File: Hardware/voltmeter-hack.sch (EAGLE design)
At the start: 18 parts, among them IC1 STM32F003F3, IC2 HT7133-1

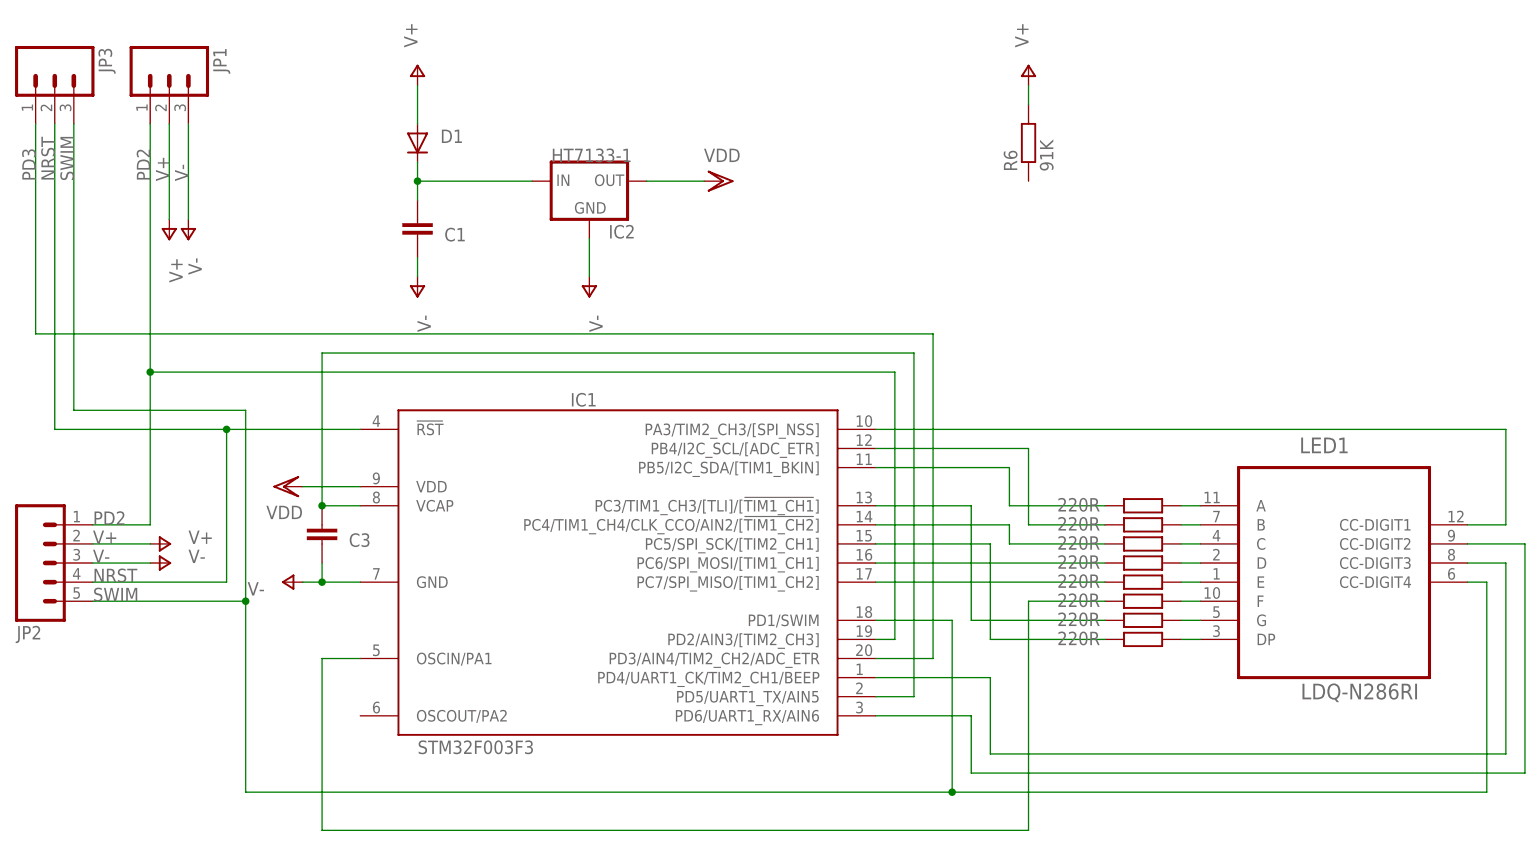
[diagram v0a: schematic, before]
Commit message: hacked voltmeter headers
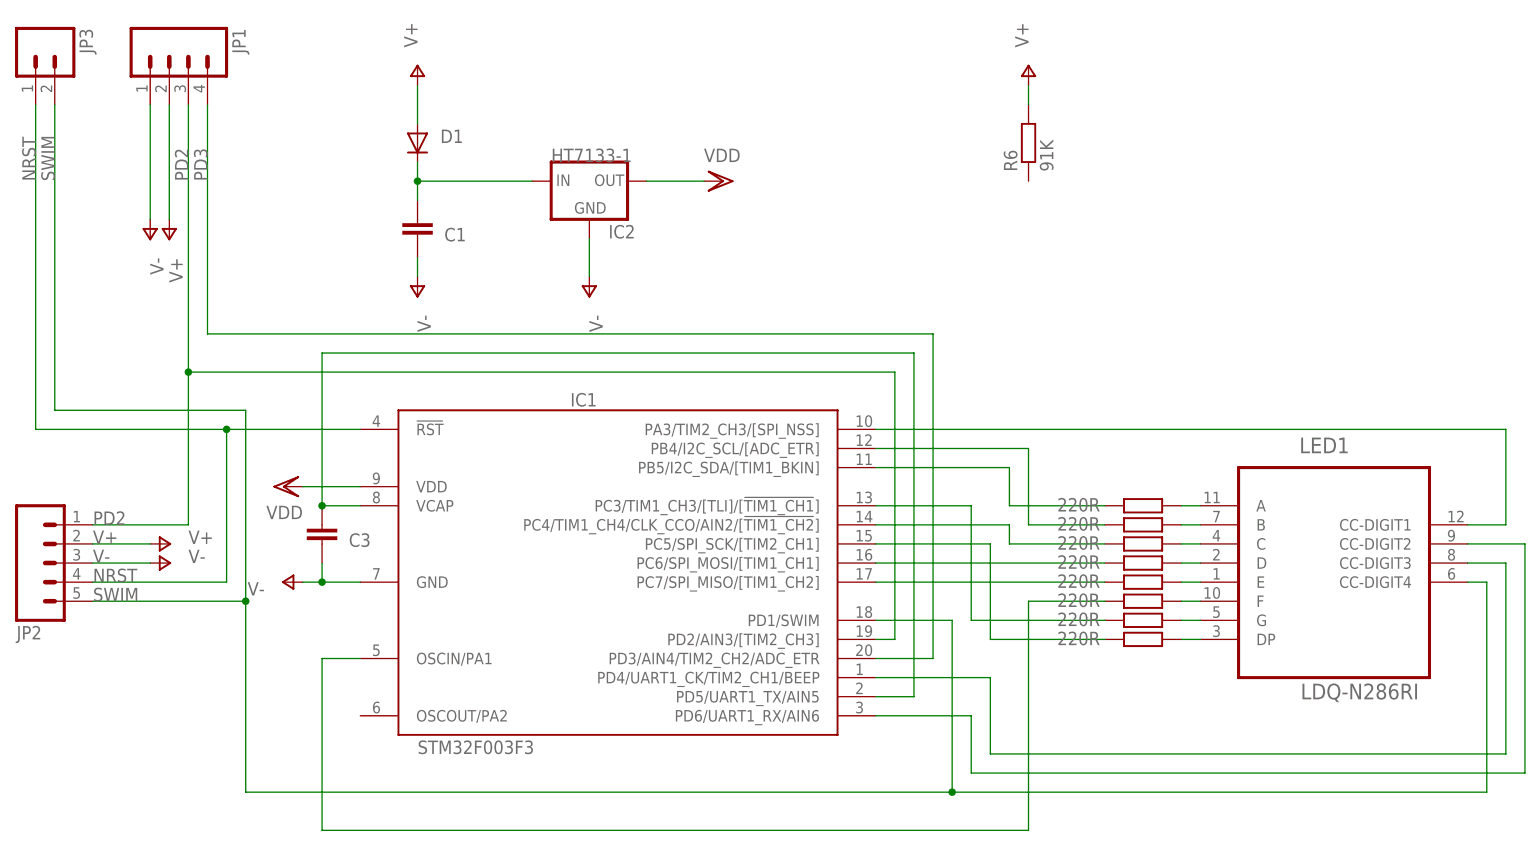
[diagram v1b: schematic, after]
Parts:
- JP1: device SparkFun:M03PTH -> SparkFun:M04PTH
- JP3: device SparkFun:M03PTH -> SparkFun:M02PTH
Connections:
- net NRST: now also JP3.1; no longer JP3.2
- net PD2: now also JP1.3; no longer JP1.1
- net PD3: now also JP1.4; no longer JP3.1
- net SWIM: now also JP3.2; no longer JP3.3
- net V-: now also JP1.1; no longer JP1.3
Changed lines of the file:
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@@
 <part name="IC1" library="stm8" deviceset="STM32F003" device="F3"/>
 <part name="LED1" library="LDQ-N286RI" deviceset="LDQ-N286RI" device=""/>
-<part name="JP1" library="SparkFun" deviceset="M03" device="PTH"/>
+<part name="JP1" library="SparkFun" deviceset="M04" device="PTH"/>
 <part name="JP2" library="SparkFun" deviceset="M05" device="PTH"/>
 <part name="D1" library="dp_devices" deviceset="DIODE" device="-SOD-123"/>
@@
 <part name="P+4" library="supply1" deviceset="V+" device=""/>
 <part name="R6" library="resistor" deviceset="R-EU_" device="R0603" value="91K"/>
-<part name="JP3" library="SparkFun" deviceset="M03" device="PTH"/>
+<part name="JP3" library="SparkFun" deviceset="M02" device="PTH"/>
 </parts>
 <sheets>
@@
 </instance>
 <instance part="VDD2" gate="G$1" x="73.66" y="78.74" rot="R270"/>
-<instance part="P-1" gate="1" x="2.54" y="71.12" smashed="yes">
-<attribute name="VALUE" x="2.54" y="68.58" size="1.778" layer="96" rot="R270"/>
+<instance part="P-1" gate="1" x="-2.54" y="71.12" smashed="yes">
+<attribute name="VALUE" x="-2.54" y="68.58" size="1.778" layer="96" rot="R270"/>
 </instance>
 <instance part="P+1" gate="1" x="0" y="71.12" smashed="yes" rot="R180">
@@
 </instance>
 <instance part="R6" gate="G$1" x="114.3" y="83.82" rot="R90"/>
-<instance part="JP3" gate="G$1" x="-15.24" y="93.98" rot="R270"/>
+<instance part="JP3" gate="G$1" x="-17.78" y="96.52" rot="R270"/>
 </instances>
 <busses>
@@
 <net name="V-" class="0">
 <segment>
-<pinref part="JP1" gate="G$1" pin="3"/>
-<wire x1="2.54" y1="86.36" x2="2.54" y2="73.66" width="0.1524" layer="91"/>
-<pinref part="P-1" gate="1" pin="V-"/>
-<label x="2.54" y="78.74" size="1.778" layer="95" rot="R90"/>
-</segment>
-<segment>
 <pinref part="P-2" gate="1" pin="V-"/>
 <pinref part="C1" gate="G$1" pin="1"/>
@@
 <junction x="20.32" y="25.4"/>
 </segment>
+<segment>
+<pinref part="P-1" gate="1" pin="V-"/>
+<pinref part="JP1" gate="G$1" pin="1"/>
+<wire x1="-2.54" y1="73.66" x2="-2.54" y2="88.9" width="0.1524" layer="91"/>
+</segment>
 </net>
 <net name="PD2" class="0">
 <segment>
-<pinref part="JP1" gate="G$1" pin="1"/>
-<wire x1="-2.54" y1="86.36" x2="-2.54" y2="53.34" width="0.1524" layer="91"/>
 <pinref part="JP2" gate="G$1" pin="1"/>
-<wire x1="-2.54" y1="53.34" x2="-2.54" y2="33.02" width="0.1524" layer="91"/>
-<wire x1="-2.54" y1="33.02" x2="-10.16" y2="33.02" width="0.1524" layer="91"/>
+<wire x1="2.54" y1="53.34" x2="2.54" y2="33.02" width="0.1524" layer="91"/>
+<wire x1="2.54" y1="33.02" x2="-10.16" y2="33.02" width="0.1524" layer="91"/>
 <label x="-10.16" y="33.02" size="1.778" layer="95"/>
 <pinref part="IC1" gate="G$1" pin="PD2/AIN3/[TIM2_CH3]"/>
 <wire x1="93.98" y1="17.78" x2="96.52" y2="17.78" width="0.1524" layer="91"/>
 <wire x1="96.52" y1="17.78" x2="96.52" y2="53.34" width="0.1524" layer="91"/>
-<wire x1="96.52" y1="53.34" x2="-2.54" y2="53.34" width="0.1524" layer="91"/>
-<junction x="-2.54" y="53.34"/>
-<label x="-2.54" y="78.74" size="1.778" layer="95" rot="R90"/>
+<wire x1="96.52" y1="53.34" x2="2.54" y2="53.34" width="0.1524" layer="91"/>
+<label x="2.54" y="78.74" size="1.778" layer="95" rot="R90"/>
+<pinref part="JP1" gate="G$1" pin="3"/>
+<wire x1="2.54" y1="88.9" x2="2.54" y2="53.34" width="0.1524" layer="91"/>
+<junction x="2.54" y="53.34"/>
 </segment>
 </net>
 <net name="V+" class="0">
-<segment>
-<pinref part="P+1" gate="1" pin="V+"/>
-<pinref part="JP1" gate="G$1" pin="2"/>
-<wire x1="0" y1="73.66" x2="0" y2="86.36" width="0.1524" layer="91"/>
-<label x="0" y="78.74" size="1.778" layer="95" rot="R90"/>
-</segment>
 <segment>
 <pinref part="P+3" gate="1" pin="V+"/>
@@
 <pinref part="P+4" gate="1" pin="V+"/>
 <wire x1="114.3" y1="88.9" x2="114.3" y2="91.44" width="0.1524" layer="91"/>
+</segment>
+<segment>
+<pinref part="JP1" gate="G$1" pin="2"/>
+<pinref part="P+1" gate="1" pin="V+"/>
+<wire x1="0" y1="88.9" x2="0" y2="73.66" width="0.1524" layer="91"/>
 </segment>
 </net>
@@
 <wire x1="7.62" y1="45.72" x2="25.4" y2="45.72" width="0.1524" layer="91"/>
 <label x="-10.16" y="25.4" size="1.778" layer="95"/>
-<pinref part="JP3" gate="G$1" pin="2"/>
-<wire x1="7.62" y1="45.72" x2="-15.24" y2="45.72" width="0.1524" layer="91"/>
-<wire x1="-15.24" y1="45.72" x2="-15.24" y2="86.36" width="0.1524" layer="91"/>
+<wire x1="7.62" y1="45.72" x2="-17.78" y2="45.72" width="0.1524" layer="91"/>
 <junction x="7.62" y="45.72"/>
-<label x="-15.24" y="78.74" size="1.778" layer="95" rot="R90"/>
+<label x="-17.78" y="78.74" size="1.778" layer="95" rot="R90"/>
+<pinref part="JP3" gate="G$1" pin="1"/>
+<wire x1="-17.78" y1="45.72" x2="-17.78" y2="88.9" width="0.1524" layer="91"/>
 </segment>
 </net>
@@
 <label x="-10.16" y="22.86" size="1.778" layer="95"/>
 <wire x1="10.16" y1="22.86" x2="10.16" y2="48.26" width="0.1524" layer="91"/>
-<pinref part="JP3" gate="G$1" pin="3"/>
-<wire x1="10.16" y1="48.26" x2="-12.7" y2="48.26" width="0.1524" layer="91"/>
-<wire x1="-12.7" y1="48.26" x2="-12.7" y2="86.36" width="0.1524" layer="91"/>
+<wire x1="10.16" y1="48.26" x2="-15.24" y2="48.26" width="0.1524" layer="91"/>
 <junction x="10.16" y="22.86"/>
-<label x="-12.7" y="78.74" size="1.778" layer="95" rot="R90"/>
+<label x="-15.24" y="78.74" size="1.778" layer="95" rot="R90"/>
+<pinref part="JP3" gate="G$1" pin="2"/>
+<wire x1="-15.24" y1="48.26" x2="-15.24" y2="88.9" width="0.1524" layer="91"/>
 </segment>
 </net>
@@
 <wire x1="93.98" y1="15.24" x2="101.6" y2="15.24" width="0.1524" layer="91"/>
 <wire x1="101.6" y1="15.24" x2="101.6" y2="58.42" width="0.1524" layer="91"/>
-<pinref part="JP3" gate="G$1" pin="1"/>
-<wire x1="101.6" y1="58.42" x2="-17.78" y2="58.42" width="0.1524" layer="91"/>
-<wire x1="-17.78" y1="58.42" x2="-17.78" y2="86.36" width="0.1524" layer="91"/>
-<label x="-17.78" y="78.74" size="1.778" layer="95" rot="R90"/>
-</segment>
-</net>
+<label x="5.08" y="78.74" size="1.778" layer="95" rot="R90"/>
+<wire x1="101.6" y1="58.42" x2="5.08" y2="58.42" width="0.1524" layer="91"/>
+<pinref part="JP1" gate="G$1" pin="4"/>
+<wire x1="5.08" y1="58.42" x2="5.08" y2="88.9" width="0.1524" layer="91"/>
+</segment>
+</net>
